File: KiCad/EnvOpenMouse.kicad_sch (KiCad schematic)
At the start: 16 parts, among them SW1 SW_Push_SPDT, SW2 SW_Push_SPDT, SW3 SW_Push_SPDT, U1 TLV70218DBVR, U2 PMW3360DM-T2QU

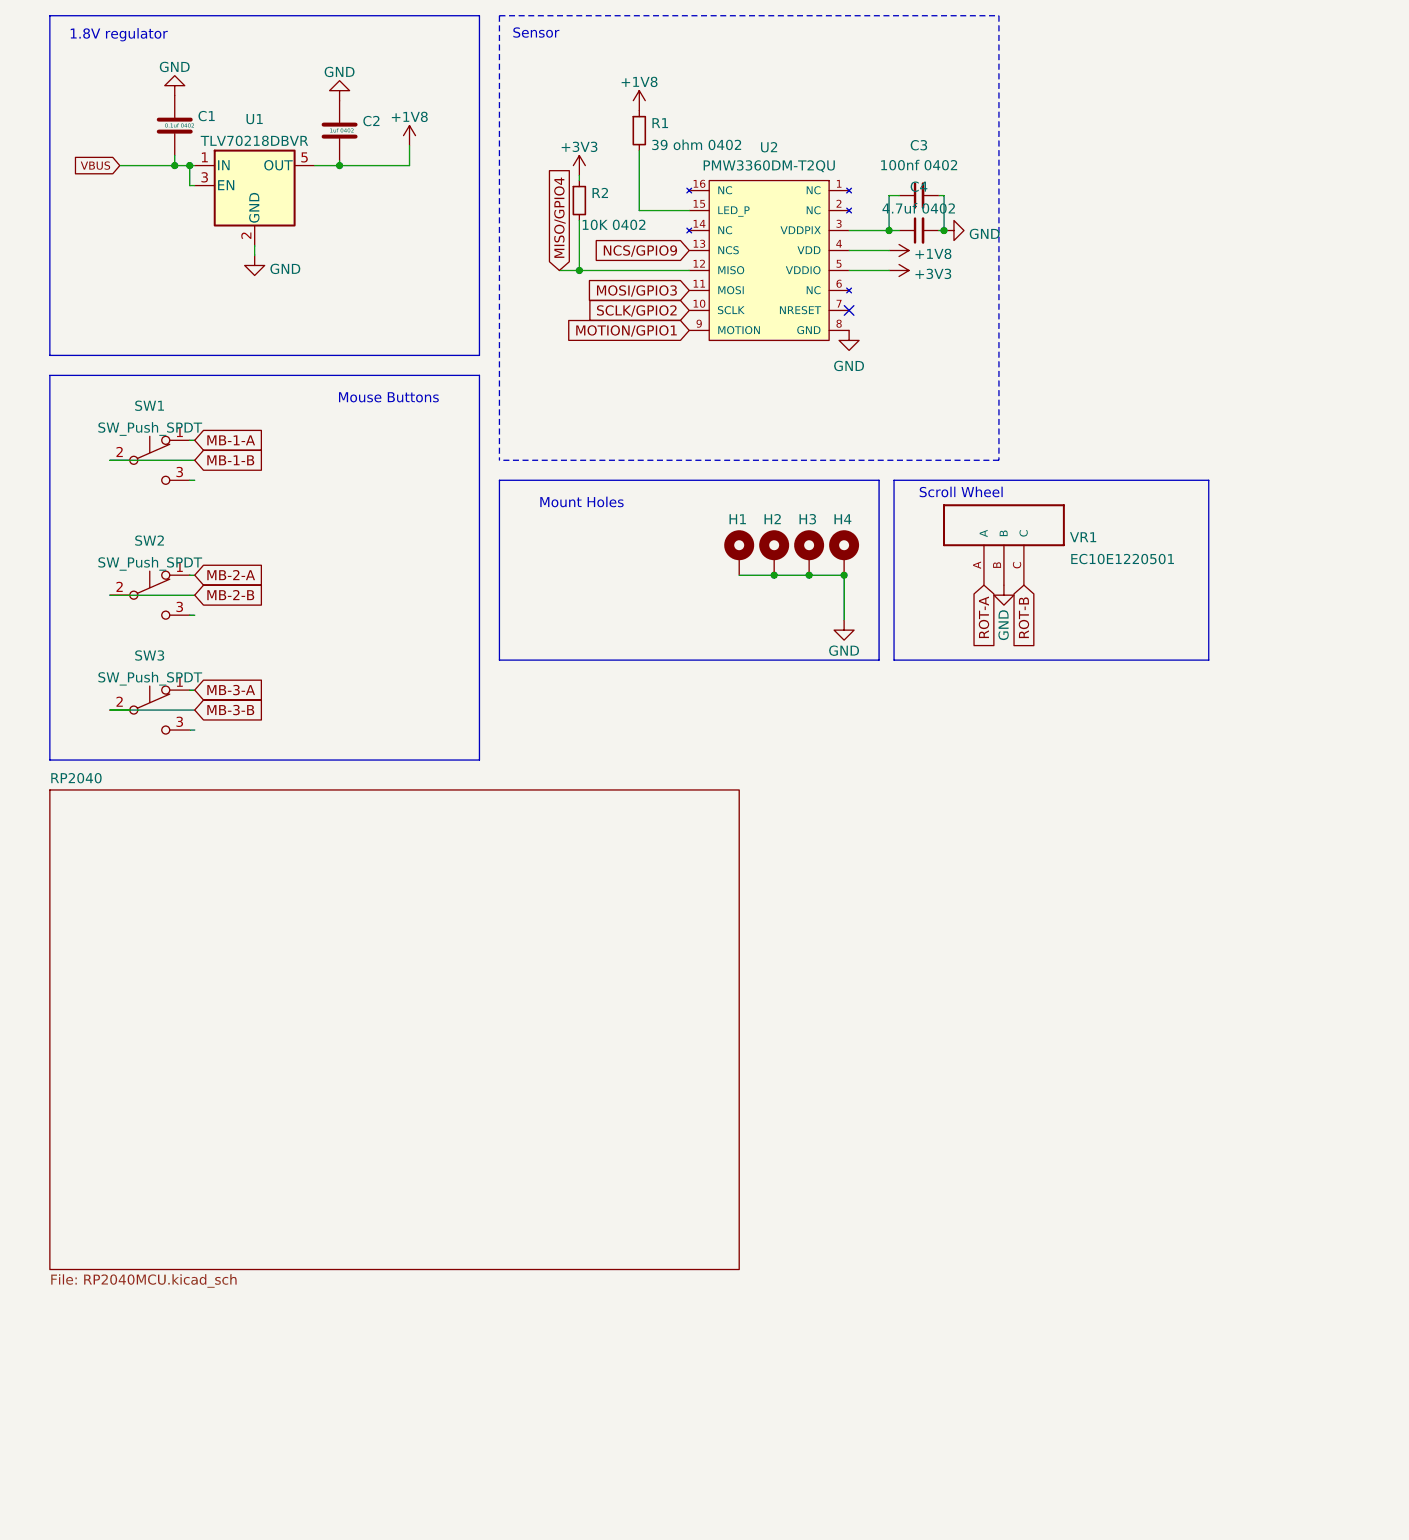
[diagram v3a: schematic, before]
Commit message: Decided to re-design the whole board again but with a pico so perhaps I can fit a PicoW and maybe make a BLE version
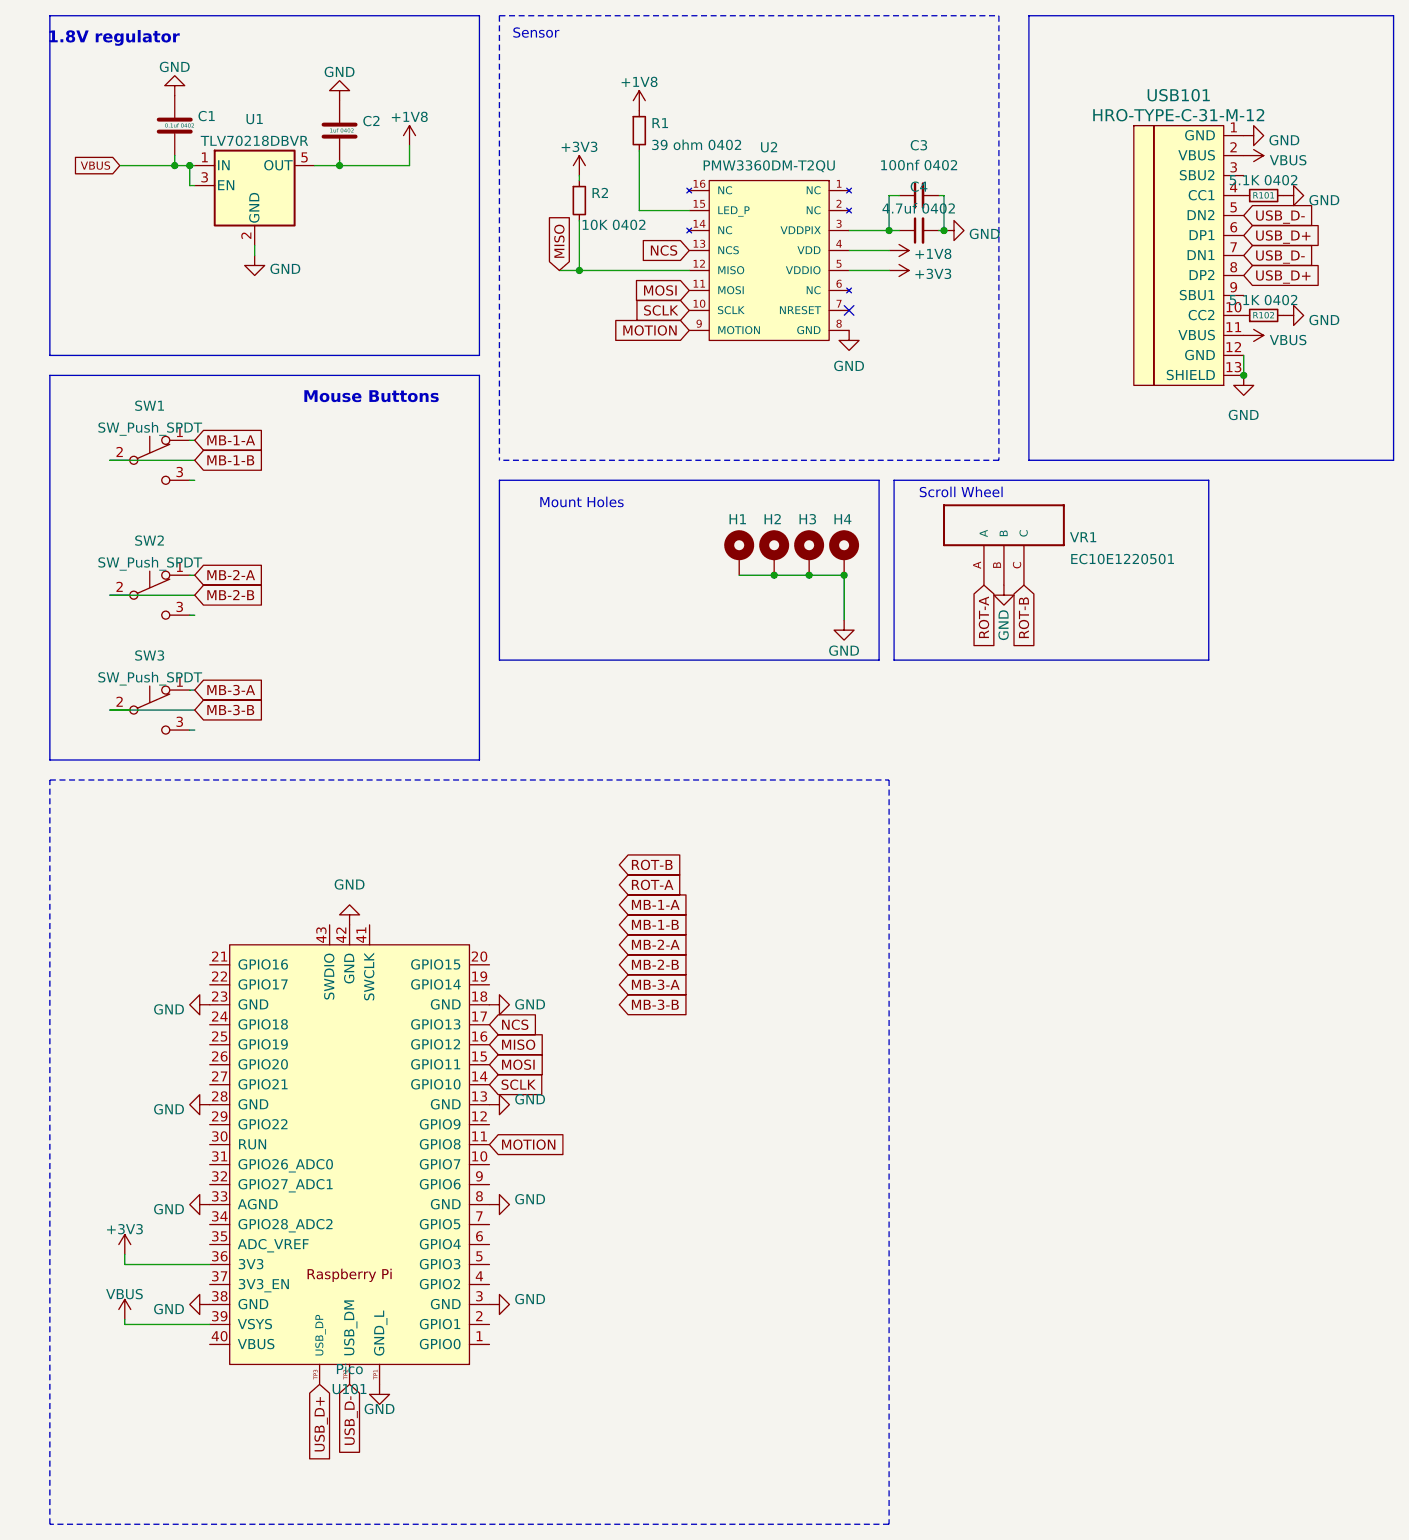
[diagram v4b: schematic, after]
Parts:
- added R101, R102: 5.1K 0402, Resistor_SMD:R_0402_1005Metric, symbol Device:R_Small
- added U101: Pico, env:RPi_Pico_SMD_TH_MODIFIED, symbol PicoModified:Pico
- added USB101: HRO-TYPE-C-31-M-12, Type-C:HRO-TYPE-C-31-M-12, symbol Type-C:HRO-TYPE-C-31-M-12
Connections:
- net +3V3: now also U101.36 (3V3)
- net GND: now also R101.2, R102.2, U101.13 (GND), U101.18 (GND), U101.23 (GND), U101.28 (GND), U101.3 (GND), U101.33 (AGND), U101.38 (GND), U101.42 (GND), U101.8 (GND), U101.TP1 (GND_L), USB101.1 (GND), USB101.12 (GND), USB101.13 (SHIELD)
- net VBUS: now also U101.39 (VSYS), USB101.11 (VBUS), USB101.2 (VBUS)
- net MISO/GPIO4 renamed MISO
- net MISO: now also U101.16 (GPIO12)
- net MOSI/GPIO3 renamed MOSI
- net MOSI: now also U101.15 (GPIO11)
- net MOTION/GPIO1 renamed MOTION
- net MOTION: now also U101.11 (GPIO8)
- net NCS/GPIO9 renamed NCS
- net NCS: now also U101.17 (GPIO13)
- net SCLK/GPIO2 renamed SCLK
- net SCLK: now also U101.14 (GPIO10)
- new net: R102.1, USB101.10 (CC2)
- new net: R101.1, USB101.4 (CC1)
- new net USB_D+: U101.TP3 (USB_DP), USB101.6 (DP1), USB101.8 (DP2)
- new net USB_D-: U101.TP2 (USB_DM), USB101.5 (DN2), USB101.7 (DN1)
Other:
- removed sheet RP2040

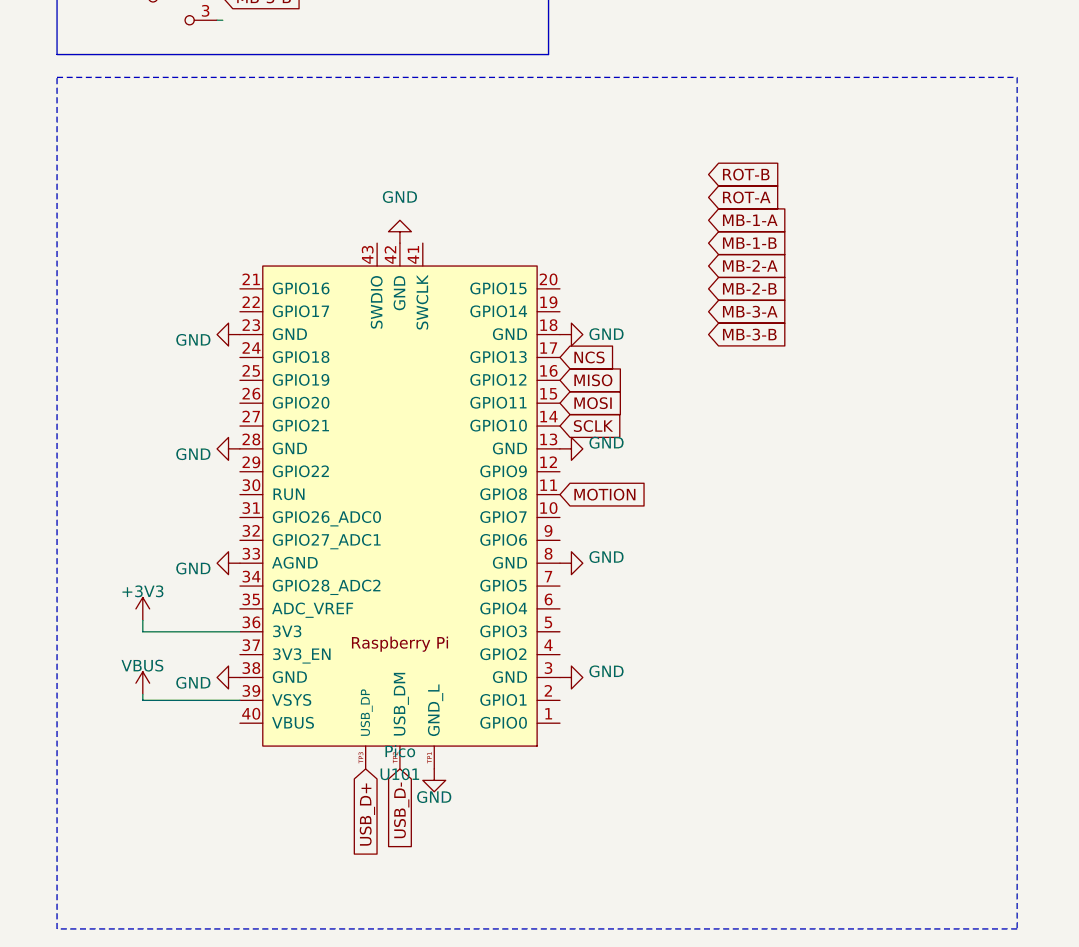
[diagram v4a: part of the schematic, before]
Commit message: routed and adjusted various traces and component positions
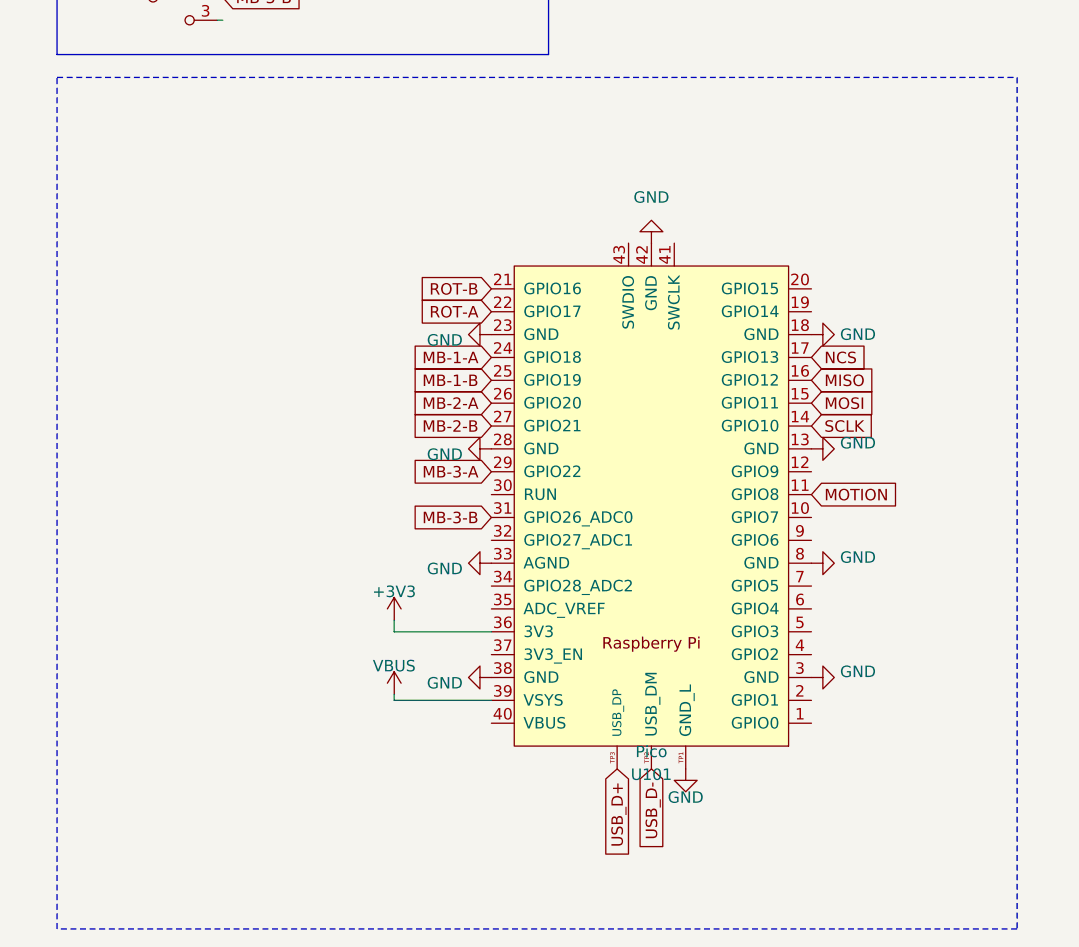
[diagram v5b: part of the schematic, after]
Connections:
- net MB-1-A: now also U101.24 (GPIO18)
- net MB-1-B: now also U101.25 (GPIO19)
- net MB-2-A: now also U101.26 (GPIO20)
- net MB-2-B: now also U101.27 (GPIO21)
- net MB-3-A: now also U101.29 (GPIO22)
- net MB-3-B: now also U101.31 (GPIO26_ADC0)
- net ROT-A: now also U101.22 (GPIO17)
- net ROT-B: now also U101.21 (GPIO16)
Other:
- moved on the sheet: U101

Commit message: overhauled design and generated gerbers
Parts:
- removed R101, R102: 5.1K 0402, Resistor_SMD:R_0402_1005Metric, symbol Device:R_Small
- removed U101: Pico, env:RPi_Pico_SMD_TH_MODIFIED, symbol PicoModified:Pico
- removed USB101: HRO-TYPE-C-31-M-12, Type-C:HRO-TYPE-C-31-M-12, symbol Type-C:HRO-TYPE-C-31-M-12
- added BT1: Li-Po Battery, Connector_JST:JST_PH_B2B-PH-K_1x02_P2.00mm_Vertical, symbol Device:Battery_Cell
- added C1: 0402 1uF, Capacitor_SMD:C_0402_1005Metric, symbol Device:C_Small
- added C10, C11, C12, C13, C14, C5, C6, C7, C8, C9: 100nf 0402, Capacitor_SMD:C_0402_1005Metric, symbol Device:C
- added C15, C16: 1uf 0402, Capacitor_SMD:C_0402_1005Metric, symbol Device:C
- added C19, C2: 22pf 0402, Capacitor_SMD:C_0402_1005Metric, symbol Device:C
- added C2: 0402 10uF, Resistor_SMD:R_0402_1005Metric, symbol Device:C_Small
- added C3: 10uf 0402 6.3V, Capacitor_SMD:C_0402_1005Metric, symbol Device:C
- added C4: 4.7uf 0402, Capacitor_SMD:C_0402_1005Metric, symbol Device:C_Small
- added C5: 10uf 0402, Capacitor_SMD:C_0402_1005Metric, symbol Device:C
- added D1: 1n4002W, Diode_SMD:D_SOD-123, symbol Device:D_Schottky
- added D2 (x2): 0402 led, LED_SMD:LED_0402_1005Metric, symbol Device:LED_Small
- added FLASH1: W25Q16JVUXIQ, Package_SON:SON-8-1EP_3x2mm_P0.5mm_EP1.4x1.6mm, symbol Memory_Flash:W25Q32JVZP
- added J2: Button, Button_Switch_SMD:SW_Push_SPST_NO_Alps_SKRK, symbol Switch:SW_Push
- added J3: Conn_01x05, Connector_PinHeader_2.54mm:PinHeader_1x05_P2.54mm_Vertical, symbol Connector_Generic:Conn_01x05
- added J4: Conn_01x09, Connector_PinHeader_2.54mm:PinHeader_1x09_P2.54mm_Vertical, symbol Connector_Generic:Conn_01x09
- added J5, J6, J7, J8: Conn_02x02_Top_Bottom, Connector_PinHeader_1.27mm:PinHeader_2x02_P1.27mm_Vertical, symbol Connector_Generic:Conn_02x02_Top_Bottom
- added J5: SKRKAEE020, Button_Switch_SMD:SW_Push_SPST_NO_Alps_SKRK, symbol Switch:SW_Push
- added J9: Conn_01x03, Connector_PinHeader_1.27mm:PinHeader_1x03_P1.27mm_Vertical, symbol Connector_Generic:Conn_01x03
- added R1, R3: 5.1K, Resistor_SMD:R_0402_1005Metric, symbol Device:R_Small
- added R1, R11: 1K 0402, Resistor_SMD:R_0402_1005Metric, symbol Device:R
- added R10, R9: 27Ohms 0402 Resistor, Capacitor_SMD:C_0402_1005Metric, symbol Device:R
- added R2: 10K 0402, Resistor_SMD:R_0402_1005Metric, symbol Device:R_Small
- added R2: 10K 0402, Resistor_SMD:R_0402_1005Metric, symbol Device:R
- added R4: 10k 0402, Resistor_SMD:R_0402_1005Metric, symbol Device:R
- added R6 (x2): 1.5K 0402, Resistor_SMD:R_0402_1005Metric, symbol Device:R_Small
- added R7: 1.13K 0402, Resistor_SMD:R_0402_1005Metric, symbol Device:R_Small
- added R7: 1.18K 0402, Resistor_SMD:R_0402_1005Metric, symbol Device:R_Small
- added R7: 4.12K 0402, Resistor_SMD:R_0402_1005Metric, symbol Device:R_Small
- added U1: TLV75733PDBVR, Package_SON:WSON-6-1EP_2x2mm_P0.65mm_EP1x1.6mm, symbol Regulator_Linear:TLV75733PDRV
- added U3: RP2040, RP2040_minimal:RP2040-QFN-56, symbol MCU_RaspberryPi_RP2040:RP2040
- added U3: BQ24074RGT, Package_DFN_QFN:VQFN-16-1EP_3x3mm_P0.5mm_EP1.6x1.6mm, symbol Battery_Management:BQ24074RGT
- added Y1: 3225_4P 12MHz, Crystal:Crystal_SMD_3225-4Pin_3.2x2.5mm, symbol Device:Crystal_GND24
- added e1: TYPE-C-31-M-12, HRO-TYPE-C31-M-12:HRO-TYPE-C-31-M-12, symbol Type-C:HRO-TYPE-C-31-M-12
- C2: renamed from C1; footprint Capacitor_SMD:C_0201_0603Metric -> Capacitor_SMD:C_0402_1005Metric
- C3: renamed from C2; footprint Capacitor_SMD:C_0201_0603Metric -> Capacitor_SMD:C_0402_1005Metric
- C8: renamed from C3; footprint Capacitor_SMD:C_0201_0603Metric -> Capacitor_SMD:C_0402_1005Metric
- C9: renamed from C4; footprint Capacitor_SMD:C_0201_0603Metric -> Capacitor_SMD:C_0402_1005Metric
- renumbered R2 to R4, U1 to U2, U2 to U4
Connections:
- net +3V3: now also C10.1, C11.1, C12.1, C13.1, C14.1, C15.1, C5.1, C5.1, C8.1, C9.1, FLASH1.8 (VCC), R2.1, U1.1 (OUT), U3.1 (IOVDD), U3.10 (IOVDD), U3.22 (IOVDD), U3.33 (IOVDD), U3.42 (IOVDD), U3.43 (ADC_AVDD), U3.44 (VREG_IN), U3.48 (USB_VDD), U3.49 (IOVDD)
- net GND: now also BT1.2 (-), C1.2, C10.2, C11.2, C12.2, C13.2, C14.2, C15.2, C16.2, C19.1, C2.1, C2.1, C3.2, C4.1, C5.2, C5.2, C6.2, C7.2, C8.2, C9.2, FLASH1.4 (GND), FLASH1.9 (EP), J2.2, J3.5 (Pin_5), J4.8 (Pin_8), J5.2, J9.2 (Pin_2), R1.1, R2.1, R3.1, R7.1, R7.2, R7.2, U1.3 (GND), U1.7 (GND), U3.14 (TMR), U3.17 (VSS), U3.19 (TESTEN), U3.4 (~{CE}), U3.5 (EN2), U3.57 (GND), U3.8 (VSS), Y1.2, Y1.4, e1.1 (GND), e1.12 (GND), e1.13 (SHIELD)
- net MB-1-A: now also J6.2 (Pin_2)
- net MB-1-B: now also J6.1 (Pin_1)
- net MB-2-A: now also J5.3 (Pin_3)
- net MB-2-B: now also J5.4 (Pin_4)
- net MB-3-A: now also J6.3 (Pin_3)
- net MB-3-B: now also J6.4 (Pin_4)
- net MISO: now also U3.15 (GPIO12)
- net MOSI: now also U3.14 (GPIO11)
- net MOTION: now also U3.12 (GPIO9)
- net NCS: now also U3.16 (GPIO13)
- net ROT-A: now also J5.2 (Pin_2)
- net ROT-B: now also J5.1 (Pin_1)
- net SCLK: now also U3.13 (GPIO10)
- net USB_D+: now also R9.1, e1.6 (DP1), e1.8 (DP2)
- net USB_D-: now also R10.1, e1.5 (DN2), e1.7 (DN1)
- net VBUS: now also D1.2 (A), e1.11 (VBUS), e1.2 (VBUS); no longer C2.2, U2.1 (IN), U2.3 (EN)
- new net: R10.2, U3.46 (USB_DM)
- new net: R9.2, U3.47 (USB_DP)
- new net: R3.2, e1.10 (CC2)
- new net: R1.2, e1.4 (CC1)
- new net: R4.2, U1.4 (EN)
- new net: R2.2, U3.1 (TS)
- new net: D2.1 (K), U3.9 (~{CHG})
- new net: D2.2 (A), R6.2 (x2)
- new net: R7.1, U3.16 (ISET)
- new net: C19.2, R11.2, Y1.3
- new net: R7.1, U3.12 (ILIM)
- new net: R7.2, U3.15 (ITERM)
- new net: D2.1 (K), U3.7 (~{PGOOD})
- new net +1V1: C16.1, C6.1, C7.1, U3.23 (DVDD), U3.45 (VREG_VOUT), U3.50 (DVDD)
- new net BLE_CS: J4.4 (Pin_4), U3.28 (GPIO17)
- new net BLE_DFU: J4.6 (Pin_6), U3.32 (GPIO21)
- new net BLE_IRQ: J4.5 (Pin_5), U3.34 (GPIO22)
- new net BLE_MISO: J4.2 (Pin_2), U3.31 (GPIO20)
- new net BLE_MOSI: J4.3 (Pin_3), U3.30 (GPIO19)
- new net BLE_RST: J4.7 (Pin_7), U3.27 (GPIO16)
- new net BLE_SCK: J4.1 (Pin_1), U3.29 (GPIO18)
- new net GPIO14: U3.17 (GPIO14)
- new net GPIO15: U3.18 (GPIO15)
- new net GPIO4: U3.6 (GPIO4)
- new net GPIO5: U3.7 (GPIO5)
- new net GPIO6: U3.8 (GPIO6)
- new net GPIO7: U3.9 (GPIO7)
- new net GPIO8: U3.11 (GPIO8)
- new net HAPTIC_SCL: J3.3 (Pin_3), U3.37 (GPIO25)
- new net HAPTIC_SDA: J3.2 (Pin_2), U3.36 (GPIO24)
- new net HAPTIC_TRIG: J3.4 (Pin_4), U3.35 (GPIO23)
- new net MB-1-A_MB: J8.2 (Pin_2), U3.39 (GPIO27_ADC1)
- new net MB-1-B_MB: J8.1 (Pin_1), U3.38 (GPIO26_ADC0)
- new net MB-2-A_MB: J7.3 (Pin_3), U3.3 (GPIO1)
- new net MB-2-B_MB: J7.4 (Pin_4), U3.2 (GPIO0)
- new net MB-3-A_MB: J8.3 (Pin_3), U3.41 (GPIO29_ADC3)
- new net MB-3-B_MB: J8.4 (Pin_4), U3.40 (GPIO28_ADC2)
- new net QSPI_SCLK: FLASH1.6 (CLK), U3.52 (QSPI_SCLK)
- new net QSPI_SD0: FLASH1.5 (DI(IO0)), U3.53 (QSPI_SD0)
- new net QSPI_SD1: FLASH1.2 (DO(IO1)), U3.55 (QSPI_SD1)
- new net QSPI_SD2: FLASH1.3 (IO2), U3.54 (QSPI_SD2)
- new net QSPI_SD3: FLASH1.7 (IO3), U3.51 (QSPI_SD3)
- new net QSPI_SS: FLASH1.1 (~{CS}), R1.1, R2.2, U3.56 (QSPI_SS)
- new net ROT-A_MB: J7.2 (Pin_2), U3.5 (GPIO3)
- new net ROT-B_MB: J7.1 (Pin_1), U3.4 (GPIO2)
- new net RUN: J5.1, U3.26 (RUN)
- new net SWCLK: J9.3 (Pin_3), U3.24 (SWCLK)
- new net SWD: J9.1 (Pin_1), U3.25 (SWD)
- new net VBAT: BT1.1 (+), C4.2, U3.2 (BAT), U3.3 (BAT)
- new net VDD: C2.2, C2.2, C3.1, J3.1 (Pin_1), J4.9 (Pin_9), R4.1, U1.6 (IN), U2.1 (IN), U2.3 (EN), U3.10 (OUT), U3.11 (OUT)
- new net VSYS: C1.1, D1.1 (K), R6.1, R6.1, U3.13 (IN), U3.6 (EN1)
- new net XIN: C2.2, U3.20 (XIN), Y1.1
- new net XOUT: R11.1, U3.21 (XOUT)
- new net ~{USB_BOOT}: J2.1, R1.2
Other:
- note added: "1K resistor to prevent overdriving of the crystal as per the minimal design example"
- note added: "2x 5.1K Resistors on the CC pins will = 5V@1.5A this is the recomended default config for type-c"
- note added: "3.3V regulator"
- note added: "Battery Charge IC"
- note added: "Crystal"
- note added: "D1 NEEDS to be 0omh resistor or 1n4002"
- note added: "Flash"
- note added: "KoreanHROParts USB_C_Receptacle_HRO_TYPE-C-31-M-12"
- note added: "Make sure C10 is close to pin 44 of RP2040"
- note added: "Make sure C3 is close to pin 45 of RP2040"
- note added: "Make sure R3 and R4 are close to RP2040"
- note added: "Make sure the flash chip you have selected supports 3.3V power or adjust the design."
- note added: "Optical Sensor"
- note added: "Pin 9 technically doesnt exist its the main central contact under the chip for heat dicipation"
- note added: "RP2040 supports 1MHz to 15MHz"
- note added: "These decoupling capacitors are meant to be put close by each 3.3V pin of the RP2040"
- note added: "USB/POWER"
- note added: "haptic module"
- note added: "not 22pf but pick to match crystal."
- note added: "this is for factory testing always pull this to ground"
- note removed: "Sensor"
- moved on the sheet: C2, C3, C8, C9, H1, H2, H3, H4, R1, R4, SW1, SW2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
